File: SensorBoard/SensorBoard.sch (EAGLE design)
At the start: 27 parts, among them IC1 7805, J1 DCJ0202, U1 CY8C5XXX-100PIN, X2 22-23-2051, X3 MINI-USB-SCHIELD-32005-201

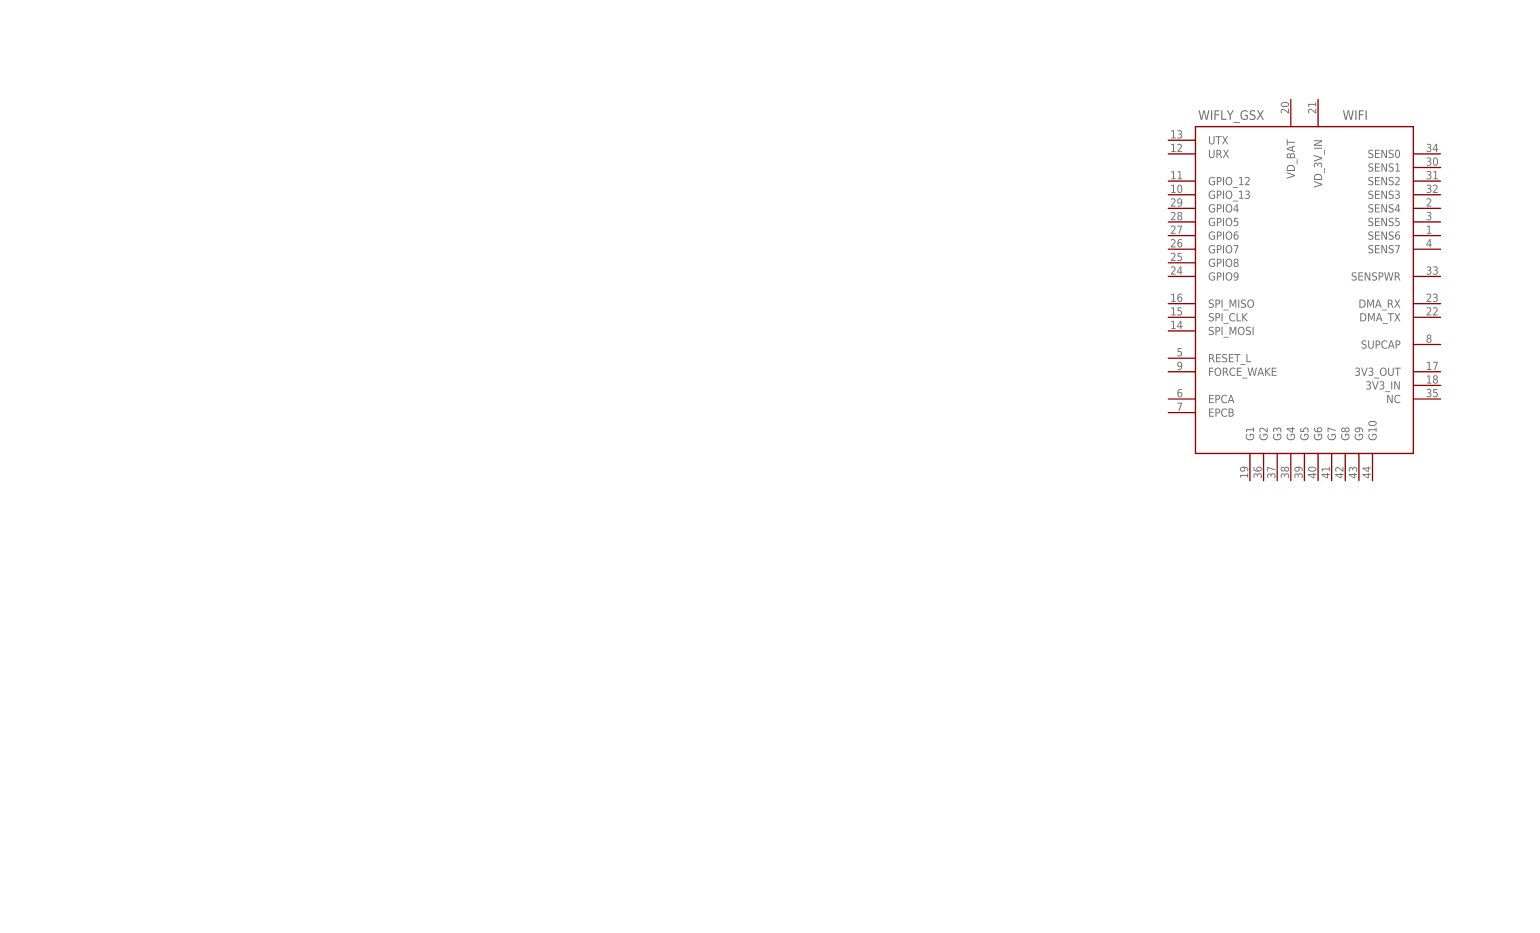
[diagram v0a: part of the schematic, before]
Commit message: wired up wifi - jack
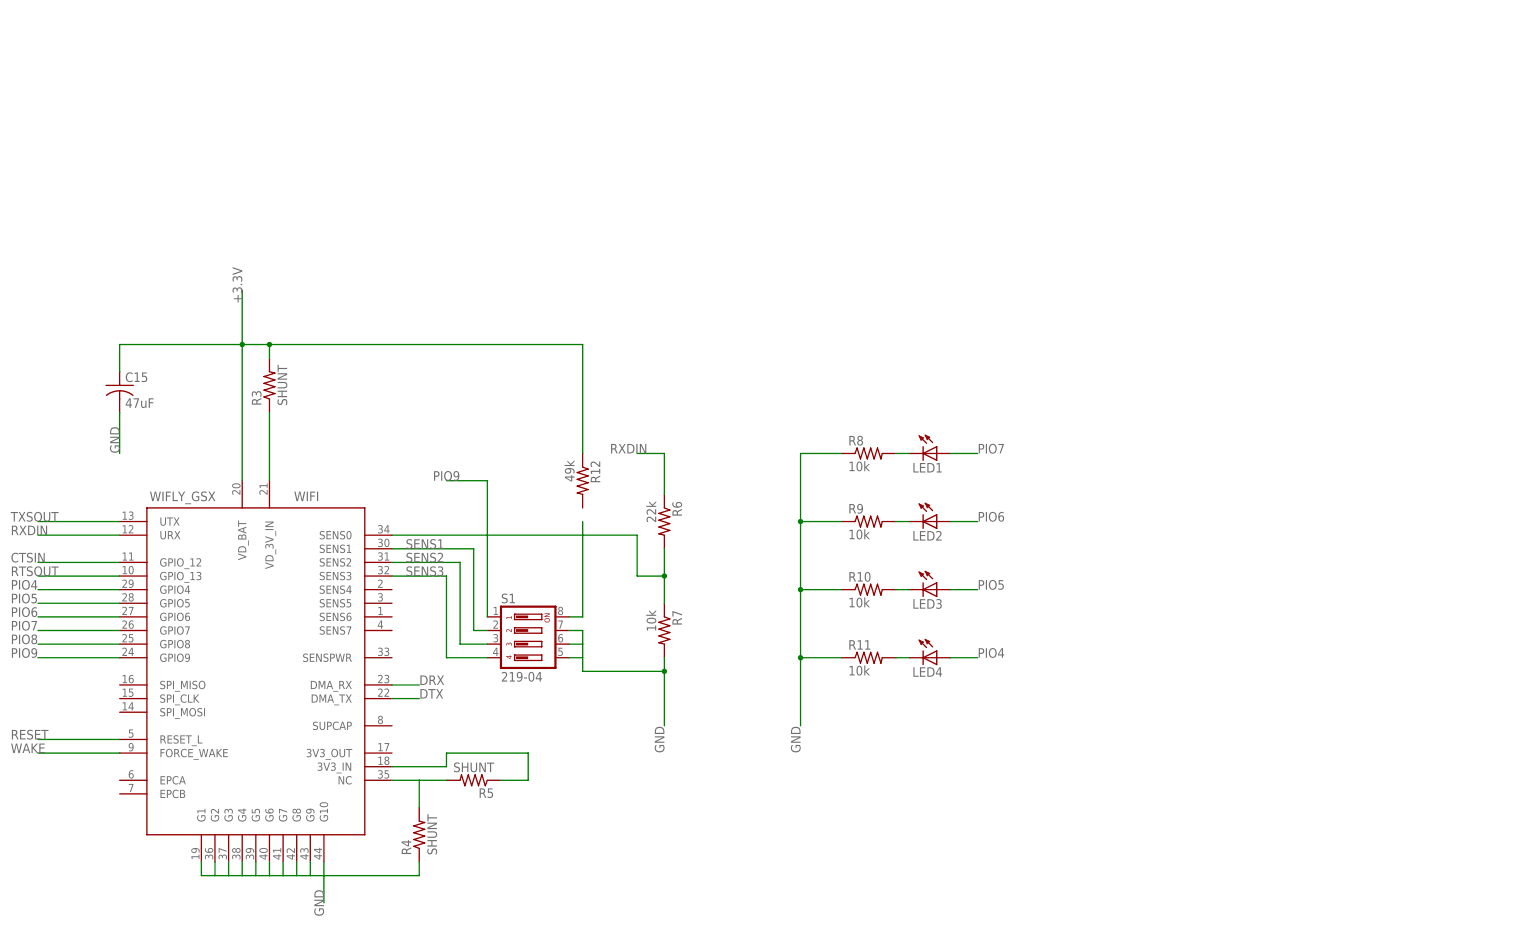
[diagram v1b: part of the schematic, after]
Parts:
- added C15: 47uF, rcl:C-USC0402
- added LED1, LED2, LED3, LED4: (no value), led:LED
- added R10, R11, R7, R8, R9: 10k, resistor:R-US_0204/5
- added R12: 49k, resistor:R-US_0204/5
- added R3, R4, R5: SHUNT, resistor:R-US_0204/5
- added R6: 22k, resistor:R-US_0204/5
- added S1: 219-04, switch-dil:219-04
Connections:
- new net CTSIN: WIFI.GPIO_12
- new net DRX: WIFI.DMA_RX
- new net DTX: WIFI.DMA_TX
- new net N$11: S1.8
- new net N$18: R3.1, WIFI.VD_3V_IN
- new net N$19: R4.2, R5.2, WIFI.NC
- new net N$20: R5.1, WIFI.3V3_IN
- new net N$23: R6.2, R7.1, WIFI.SENS0
- new net N$4: LED1.C, R8.2
- new net N$7: LED2.C, R9.2
- new net N$8: LED3.C, R10.2
- new net N$9: LED4.C, R11.2
- new net PIO4: LED4.A, WIFI.GPIO4
- new net PIO5: LED3.A, WIFI.GPIO5
- new net PIO6: LED2.A, WIFI.GPIO6
- new net PIO7: LED1.A, WIFI.GPIO7
- new net PIO8: WIFI.GPIO8
- new net PIO9: S1.1, WIFI.GPIO9
- new net RESET: WIFI.RESET_L
- new net RTSOUT: WIFI.GPIO_13
- new net RXDIN: R6.1, WIFI.URX
- new net SENS1: S1.2, WIFI.SENS1
- new net SENS2: S1.3, WIFI.SENS2
- new net SENS3: S1.4, WIFI.SENS3
- new net TXSOUT: WIFI.UTX
- new net WAKE: WIFI.FORCE_WAKE
- net +3.3V: now also C15.1, R12.1, R3.2, WIFI.VD_BAT
- net GND: now also C15.2, R10.1, R11.1, R4.1, R7.2, R8.1, R9.1, S1.5, S1.6, S1.7, WIFI.G1, WIFI.G10, WIFI.G2, WIFI.G3, WIFI.G4, WIFI.G5, WIFI.G6, WIFI.G7, WIFI.G8, WIFI.G9
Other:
- moved on the sheet: WIFI

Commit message: added stuff to board
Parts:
- removed ACCELEROMETER: MPU-6000QFN-24, SparkFun-Sensors:MPU-6000QFN-24
- removed C15: 47uF, rcl:C-USC0402
- removed GPS: COPERNICUSSMD, SparkFun-RF:COPERNICUSSMD
- removed LED1, LED2, LED3, LED4: (no value), led:LED
- removed R10, R11, R7, R8, R9: 10k, resistor:R-US_0204/5
- removed R12: 49k, resistor:R-US_0204/5
- removed R3, R4, R5: SHUNT, resistor:R-US_0204/5
- removed R6: 22k, resistor:R-US_0204/5
- removed S1: 219-04, switch-dil:219-04
- removed WIFI: WIFLY_GSX, SparkFun-RF:WIFLY_GSX
- added GPS1, GPS2, GPS3, GPS4: COPERNICUSSMD, SparkFun-RF:COPERNICUSSMD
- added U$1, U$2, U$3, U$4: ANTENNA2SMD, SparkFun-RF:ANTENNA2SMD
- added X1, X4, X5, X6: 22-23-2041, con-molex:22-23-2041
- renumbered U1 to CY8C5868AXI-LP035
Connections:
- removed net CTSIN: WIFI.GPIO_12
- removed net DRX: WIFI.DMA_RX
- removed net DTX: WIFI.DMA_TX
- removed net N$11: S1.8
- removed net N$18: R3.1, WIFI.VD_3V_IN
- removed net N$19: R4.2, R5.2, WIFI.NC
- removed net N$20: R5.1, WIFI.3V3_IN
- removed net N$23: R6.2, R7.1, WIFI.SENS0
- removed net N$4: LED1.C, R8.2
- removed net N$7: LED2.C, R9.2
- removed net N$8: LED3.C, R10.2
- removed net N$9: LED4.C, R11.2
- removed net PIO4: LED4.A, WIFI.GPIO4
- removed net PIO5: LED3.A, WIFI.GPIO5
- removed net PIO6: LED2.A, WIFI.GPIO6
- removed net PIO7: LED1.A, WIFI.GPIO7
- removed net PIO8: WIFI.GPIO8
- removed net PIO9: S1.1, WIFI.GPIO9
- removed net RESET: WIFI.RESET_L
- removed net RTSOUT: WIFI.GPIO_13
- removed net RXDIN: R6.1, WIFI.URX
- removed net SENS1: S1.2, WIFI.SENS1
- removed net SENS2: S1.3, WIFI.SENS2
- removed net SENS3: S1.4, WIFI.SENS3
- removed net TXSOUT: WIFI.UTX
- removed net WAKE: WIFI.FORCE_WAKE
- new net GPS1RXA: GPS1.RXD-A
- new net GPS1RXB: GPS1.RXD-B
- new net GPS1TXA: GPS1.TXD-A
- new net GPS1TXB: GPS1.RESERVED5
- new net GPS1XSTB: GPS1.XSTANDBY
- new net GPS2RXA: GPS2.RXD-A
- new net GPS2RXB: GPS2.RXD-B
- new net GPS2TXA: GPS2.TXD-A
- new net GPS2TXB: GPS2.RESERVED5
- new net GPS2XSTB: GPS2.XSTANDBY
- new net GPS3RXA: GPS3.RXD-A
- new net GPS3RXB: GPS3.RXD-B
- new net GPS3TXA: GPS3.TXD-A
- new net GPS3TXB: GPS3.RESERVED5
- new net GPS3XSTB: GPS3.XSTANDBY
- new net GPS4RXA: GPS4.RXD-A
- new net GPS4RXB: GPS4.RXD-B
- new net GPS4TXA: GPS4.TXD-A
- new net GPS4TXB: GPS4.RESERVED5
- new net GPS4XSTB: GPS4.XSTANDBY
- new net N$10: GPS1.RFIN, U$1.SIGNAL
- new net N$12: GPS2.RFIN, U$2.SIGNAL
- new net N$13: GPS3.RFIN, U$3.SIGNAL
- new net N$14: GPS4.RFIN, U$4.SIGNAL
- new net RX1: X1-4.S
- new net RX2: X4-4.S
- new net RX3: X5-4.S
- new net RX4: X6-4.S
- new net TX1: X1-3.S
- new net TX2: X4-3.S
- new net TX3: X5-3.S
- new net TX4: X6-3.S
- net +3.3V: now also GPS1.VCC, GPS2.VCC, GPS3.VCC, GPS4.VCC; no longer C15.1, R12.1, R3.2, WIFI.VD_BAT
- net +5V: now also X1-2.S, X4-2.S, X5-2.S, X6-2.S
- net GND: now also GPS1.GND@1, GPS1.GND@2, GPS1.GND@3, GPS1.GND@4, GPS1.GND@5, GPS1.GND@6, GPS1.GND@7, GPS1.GND@8, GPS1.OPEN, GPS2.GND@1, GPS2.GND@2, GPS2.GND@3, GPS2.GND@4, GPS2.GND@5, GPS2.GND@6, GPS2.GND@7, GPS2.GND@8, GPS2.OPEN, GPS3.GND@1, GPS3.GND@2, GPS3.GND@3, GPS3.GND@4, GPS3.GND@5, GPS3.GND@6, GPS3.GND@7, GPS3.GND@8, GPS3.OPEN, GPS4.GND@1, GPS4.GND@2, GPS4.GND@3, GPS4.GND@4, GPS4.GND@5, GPS4.GND@6, GPS4.GND@7, GPS4.GND@8, GPS4.OPEN, X1-1.S, X4-1.S, X5-1.S, X6-1.S; no longer C15.2, R10.1, R11.1, R4.1, R7.2, R8.1, R9.1, S1.5, S1.6, S1.7, WIFI.G1, WIFI.G10, WIFI.G2, WIFI.G3, WIFI.G4, WIFI.G5, WIFI.G6, WIFI.G7, WIFI.G8, WIFI.G9

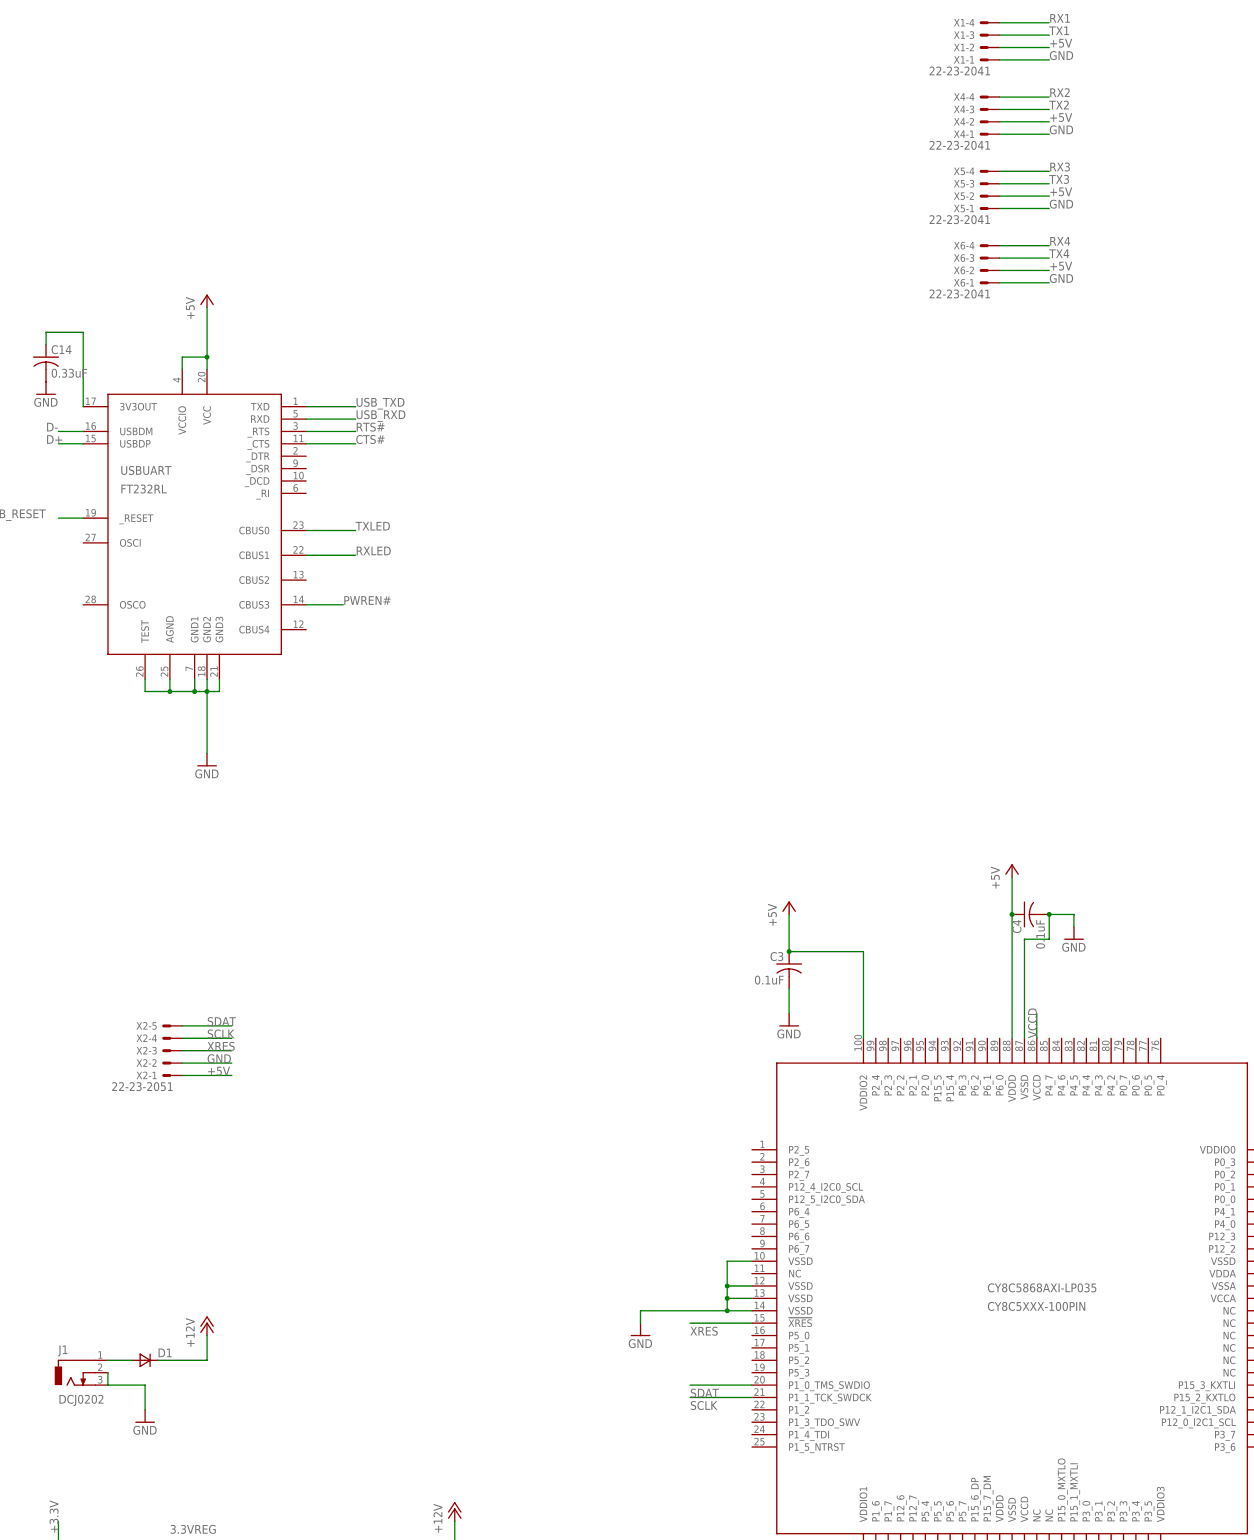
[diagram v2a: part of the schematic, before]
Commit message: wired up gps
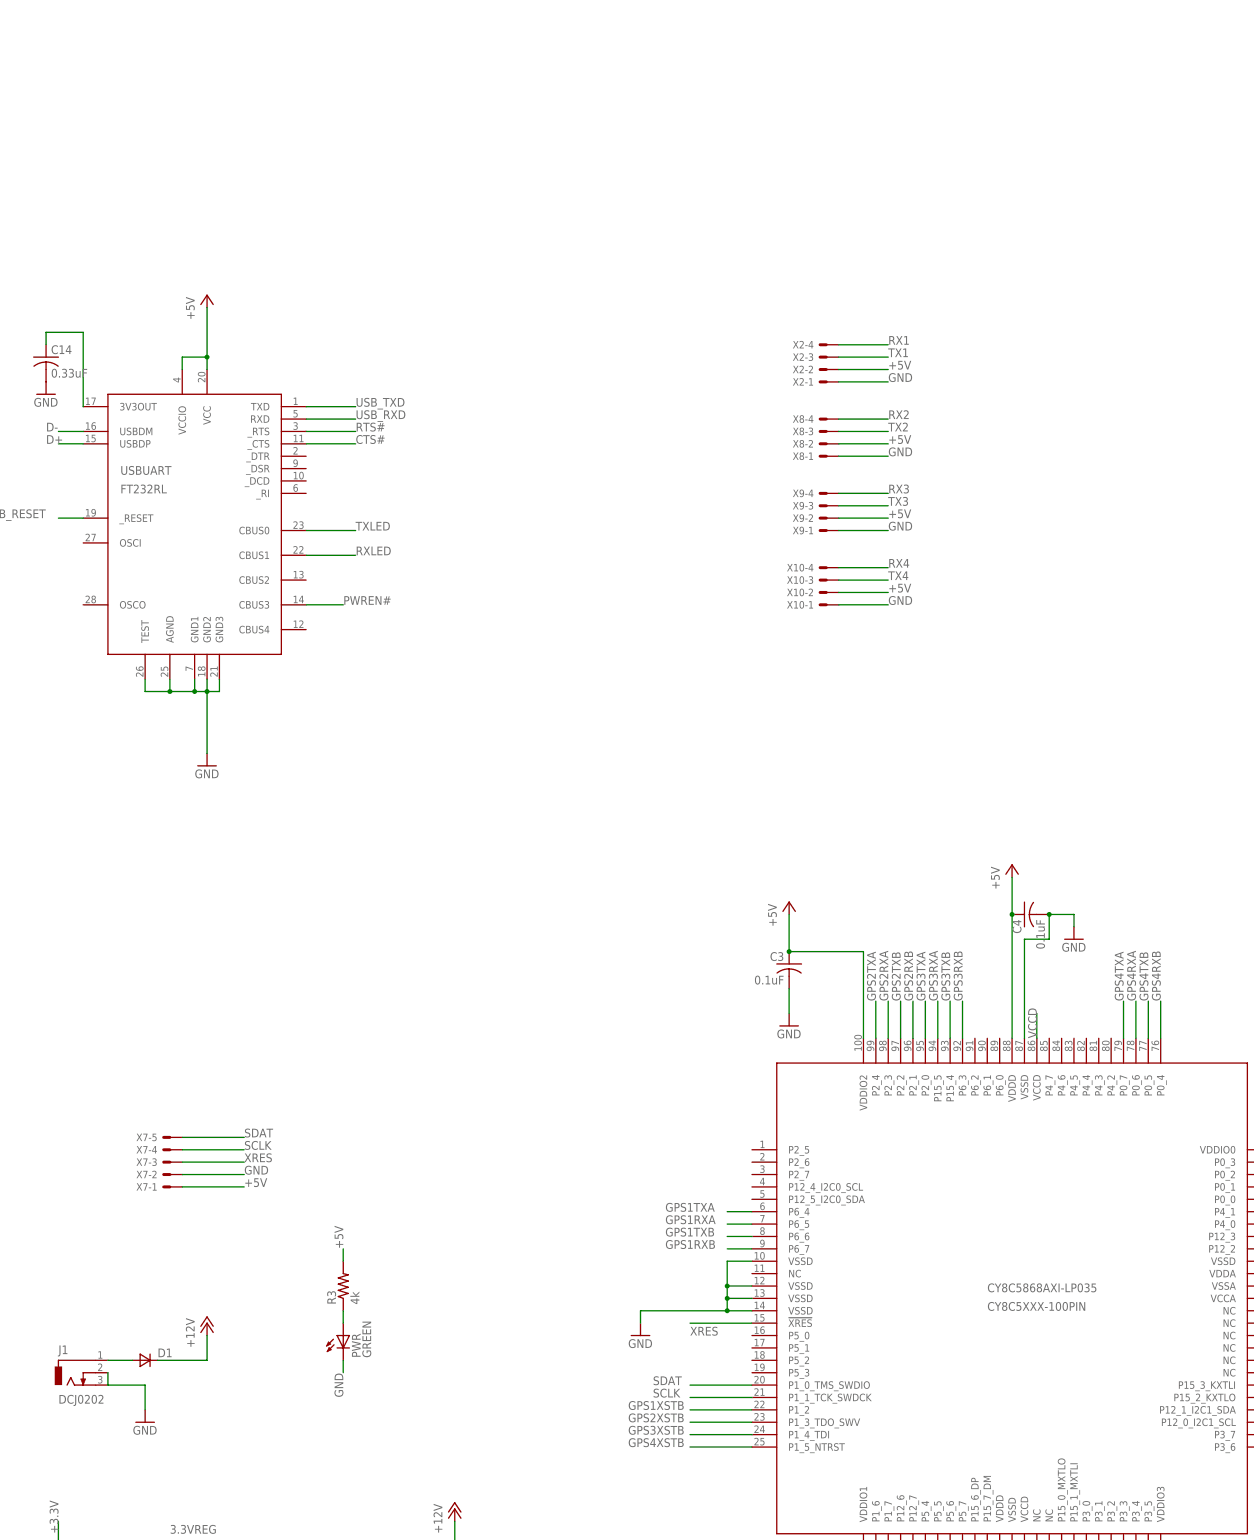
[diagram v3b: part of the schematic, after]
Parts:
- removed X1, X4, X5, X6: 22-23-2041, con-molex:22-23-2041
- added PWR: GREEN, led:LED
- added R3: 4k, resistor:R-US_0204/5
- added X10, X8, X9: (no value), con-molex:KK-156-4
- added X7: (no value), con-molex:KK-156-5
- X2: value 22-23-2051 -> (none); device con-molex:22-23-2051 -> con-molex:KK-156-4
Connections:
- new net N$4: PWR.A, R3.1
- net +5V: now also R3.2, X10-2.S, X2-2.S, X7-1.S, X8-2.S, X9-2.S; no longer X1-2.S, X2-1.S, X4-2.S, X5-2.S, X6-2.S
- net GND: now also PWR.C, X10-1.S, X2-1.S, X7-2.S, X8-1.S, X9-1.S; no longer X1-1.S, X2-2.S, X4-1.S, X5-1.S, X6-1.S
- net GPS1RXA: now also CY8C5868AXI-LP035.P6_5
- net GPS1RXB: now also CY8C5868AXI-LP035.P6_7
- net GPS1TXA: now also CY8C5868AXI-LP035.P6_4
- net GPS1TXB: now also CY8C5868AXI-LP035.P6_6
- net GPS1XSTB: now also CY8C5868AXI-LP035.P1_2
- net GPS2RXA: now also CY8C5868AXI-LP035.P2_3
- net GPS2RXB: now also CY8C5868AXI-LP035.P2_1
- net GPS2TXA: now also CY8C5868AXI-LP035.P2_4
- net GPS2TXB: now also CY8C5868AXI-LP035.P2_2
- net GPS2XSTB: now also CY8C5868AXI-LP035.P1_3_TDO_SWV
- net GPS3RXA: now also CY8C5868AXI-LP035.P15_5
- net GPS3RXB: now also CY8C5868AXI-LP035.P6_3
- net GPS3TXA: now also CY8C5868AXI-LP035.P2_0
- net GPS3TXB: now also CY8C5868AXI-LP035.P15_4
- net GPS3XSTB: now also CY8C5868AXI-LP035.P1_4_TDI
- net GPS4RXA: now also CY8C5868AXI-LP035.P0_6
- net GPS4RXB: now also CY8C5868AXI-LP035.P0_4
- net GPS4TXA: now also CY8C5868AXI-LP035.P0_7
- net GPS4TXB: now also CY8C5868AXI-LP035.P0_5
- net GPS4XSTB: now also CY8C5868AXI-LP035.P1_5_NTRST
- net RX1: now also X2-4.S; no longer X1-4.S
- net RX2: now also X8-4.S; no longer X4-4.S
- net RX3: now also X9-4.S; no longer X5-4.S
- net RX4: now also X10-4.S; no longer X6-4.S
- net SCLK: now also X7-4.S; no longer X2-4.S
- net SDAT: now also X7-5.S; no longer X2-5.S
- net TX1: now also X2-3.S; no longer X1-3.S
- net TX2: now also X8-3.S; no longer X4-3.S
- net TX3: now also X9-3.S; no longer X5-3.S
- net TX4: now also X10-3.S; no longer X6-3.S
- net XRES: now also X7-3.S; no longer X2-3.S
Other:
- moved on the sheet: X2-1, X2-2, X2-3, X2-4
